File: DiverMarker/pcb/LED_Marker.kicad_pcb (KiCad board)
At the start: 2 copper layers, 105 x 24 mm, 26 parts, among them IC101 PIC16LF15313, J101 SKEDD6, Q100 Q_NPN_Darlington, Q101 Q_NPN_Darlington, SW101 MK15-C2

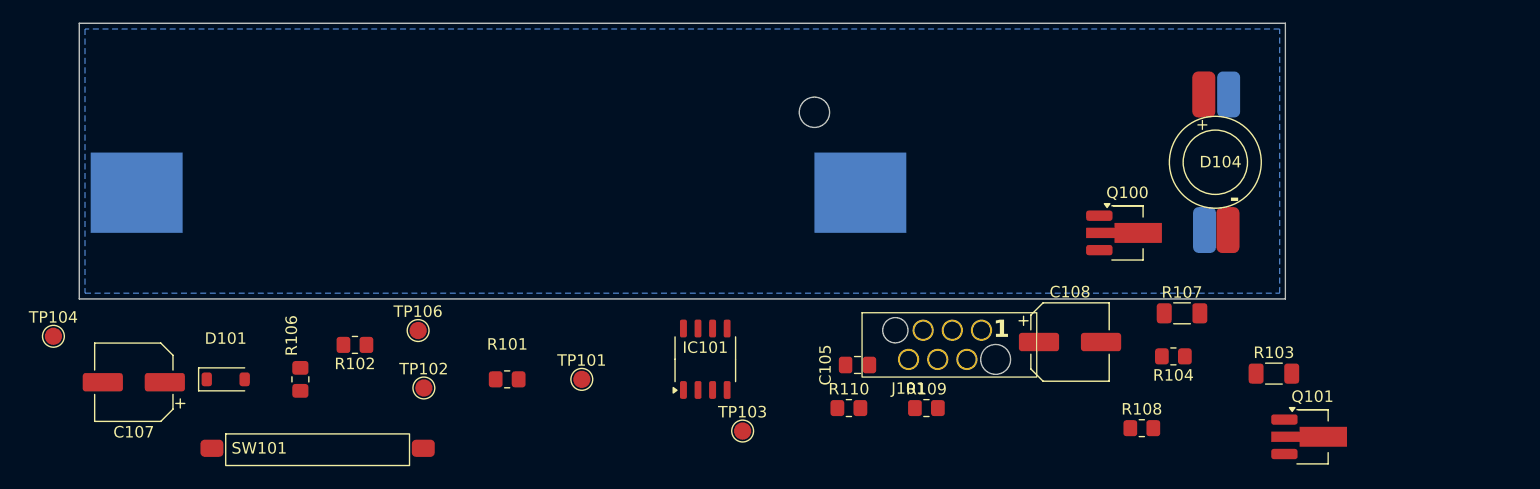
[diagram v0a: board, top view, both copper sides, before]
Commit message: Routing PCB diver marker started; almost ready but a least of open drc errors.
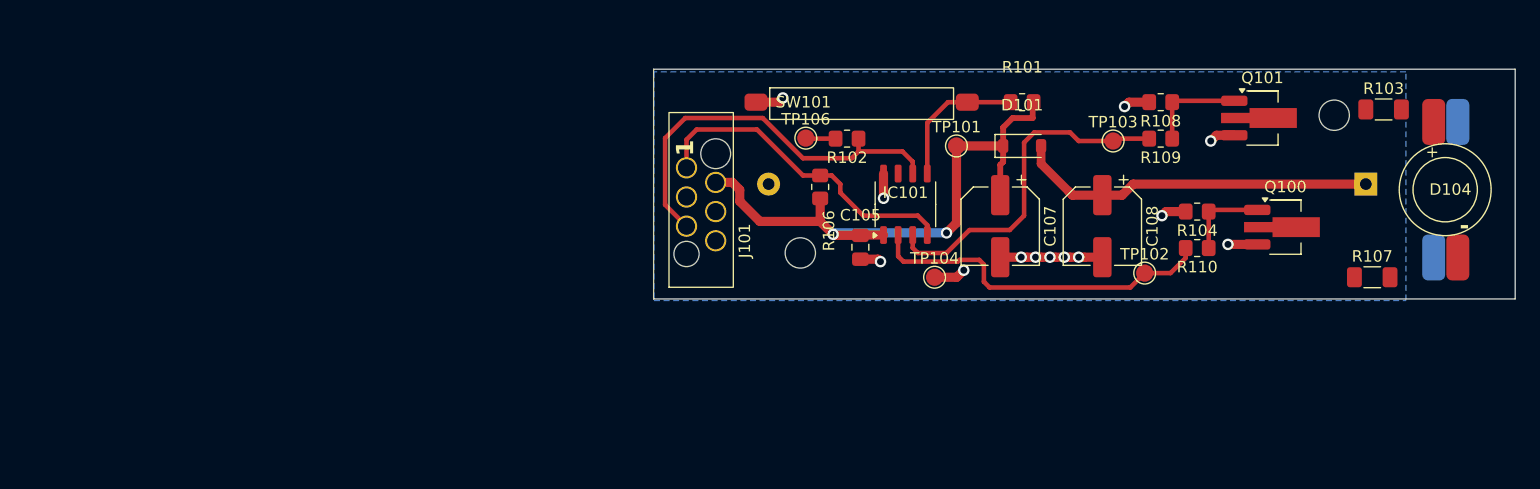
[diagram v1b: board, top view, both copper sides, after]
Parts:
- removed BAT101: KEYSTONE Battery Holder 1024, MyPower:KEYSTONE_1024
- added BT101: Keystone 2460, Battery:BatteryHolder_Keystone_2460_1xAA, B.Cu at (162.0, 110.0)
- D103: value LB-P200B2C-H -> LB-P200B2C-H, blue
- D104: value LB-P200G3C-H -> LB-P200G3C-H, green
- Q100, Q101: value Q_NPN_Darlington -> BST-52
- moved TP104 76.9 mm to (124.5, 118.1)
- moved C107 76.6 mm to (130.2, 113.7), turned to -90 degrees
- moved D101 72.2 mm to (132.1, 106.7)
- moved TP102 63.5 mm to (142.8, 117.8)
- moved SW101 56.1 mm to (118.1, 102.9)
- moved R101 50.9 mm to (132.1, 102.9)
- moved R106 48.3 mm to (114.5, 110.2), turned to 90 degrees
- moved R102 46.5 mm to (116.8, 106.0)
- moved TP103 41.0 mm to (140.0, 106.2)
- moved TP101 38.4 mm to (126.4, 106.7)
- moved TP106 37.7 mm to (113.2, 106.0)
- moved R110 33.4 mm to (147.3, 115.6), turned to 180 degrees
- moved R109 31.1 mm to (144.1, 106.0), turned to 180 degrees
- moved J101 29.3 mm to (102.9, 108.6), turned to 90 degrees
- moved R108 28.4 mm to (144.1, 102.9), turned to 180 degrees
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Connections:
- net Net-(D103-A) renamed /A_D103
- net Net-(D103-K) renamed /K_D013
- net Net-(D104-A) renamed /A_D104
- net Net-(D104-K) renamed /K_D104
- net Net-(Q100-B) renamed /BQ100
- net Net-(Q101-B) renamed /BQ101
- IC101 pad 2: GreenOn -> BlueOn
- IC101 pad 3: BlueOn -> GreenOn
- TP102 pad 1: GreenOn -> BlueOn
- TP103 pad 1: BlueOn -> GreenOn
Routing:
- net /PWR_MCU: track 0.00 -> 51.4 mm, vias 0 -> 2
- net /ICSPCLK: track 0.00 -> 34.9 mm
- net +BATT: track 0.00 -> 31.5 mm
- net BlueOn: track 0.00 -> 30.9 mm
- net GreenOn: track 0.00 -> 30.4 mm
- net /MCLR!: track 0.00 -> 28.5 mm
- net GND: track 0.00 -> 27.5 mm, vias 0 -> 13
- net /Reed_In: track 0.00 -> 12.4 mm
- net /BQ101: track 0.00 -> 8.63 mm
- net /BQ100: track 0.00 -> 7.47 mm
- net /DEBUG: track 0.00 -> 2.61 mm
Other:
- board size 105 x 24 mm -> 75 x 20 mm

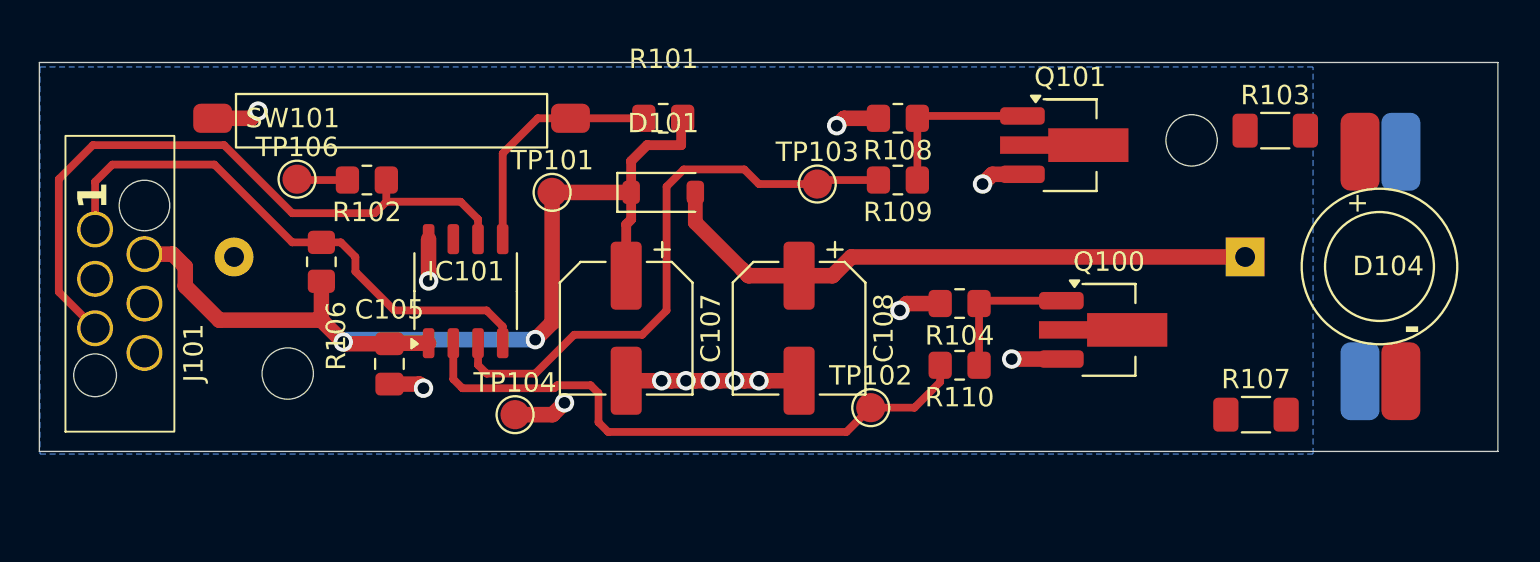
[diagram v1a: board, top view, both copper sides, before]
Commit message: pcb finished errors almost removed
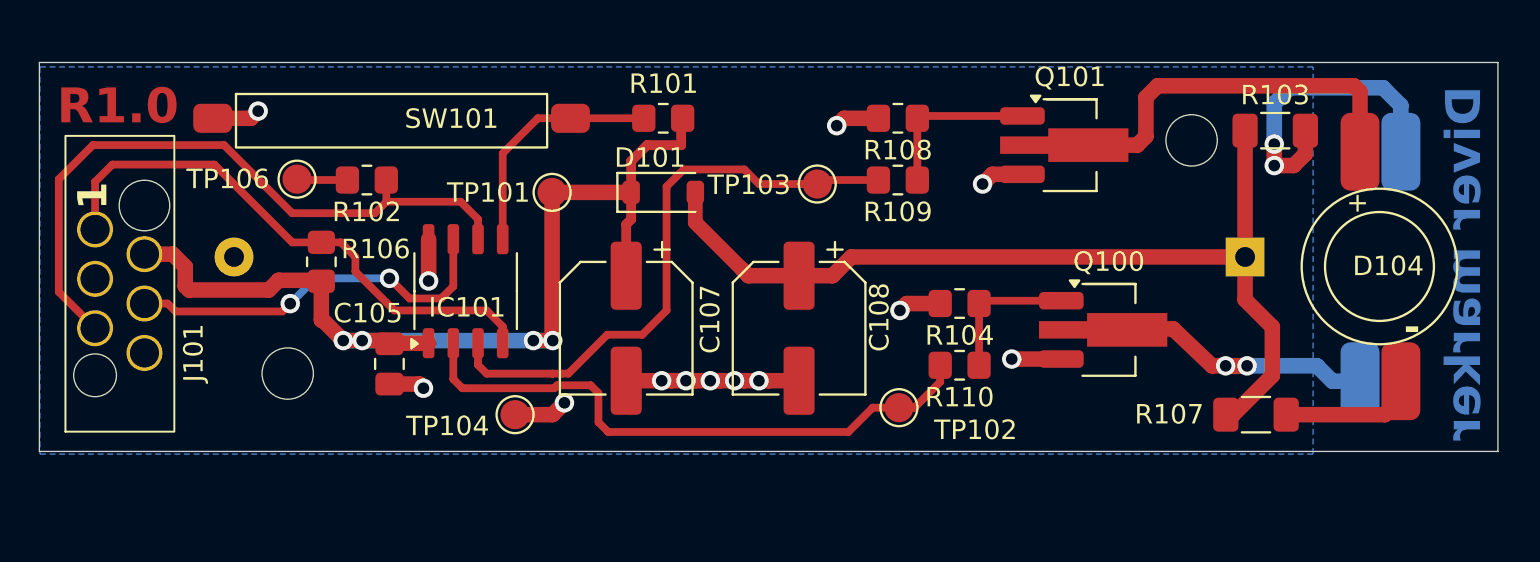
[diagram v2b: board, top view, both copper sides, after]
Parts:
- moved TP102 1.45 mm to (144.2, 117.8)
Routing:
- net /K_D104: track 0.00 -> 22.9 mm
- net /ICSPDAT: track 0.00 -> 20.0 mm, vias 0 -> 2
- net /K_D013: track 0.00 -> 17.5 mm, vias 0 -> 2
- net /A_D103: track 0.00 -> 16.9 mm, vias 0 -> 2
- net +BATT: track 31.5 -> 47.9 mm
- net /A_D104: track 0.00 -> 7.14 mm
- net /PWR_MCU: track 51.4 -> 52.4 mm, vias 2 -> 4
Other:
- board text added: "Diver marker"
- board text added: "R1.0"
